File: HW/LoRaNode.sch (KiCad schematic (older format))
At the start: 3 parts

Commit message: update some schematic design
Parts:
- added C1, C2, C3, C5: 100nF, Capacitor_SMD:C_0402_1005Metric, symbol pspice:CAP
- added C4: 4u7, Capacitor_SMD:C_0603_1608Metric, symbol pspice:CAP
- added J1: Conn_ARM_JTAG_SWD_10, Connector_PinHeader_1.27mm:PinHeader_2x05_P1.27mm_Vertical_SMD, symbol Connector:Conn_ARM_JTAG_SWD_10
- added R1, R2, R3: 0, Resistor_SMD:R_0402_1005Metric, symbol Device:R
- U3: renamed from U?; footprint (none) -> Package_SO:SO-8_3.9x4.9mm_P1.27mm
- gave numbers to parts that had none: 2
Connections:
- net labels added: GND, NRST, SPI1_CLK, SPI1_MISO, SPI1_MOSI, SPI1_NSS, SPI1_SCLK, SWDCLK, SWDIO
- wire segments 0 -> 42
- no-connect marks 0 -> 3
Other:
- moved on the sheet: U2

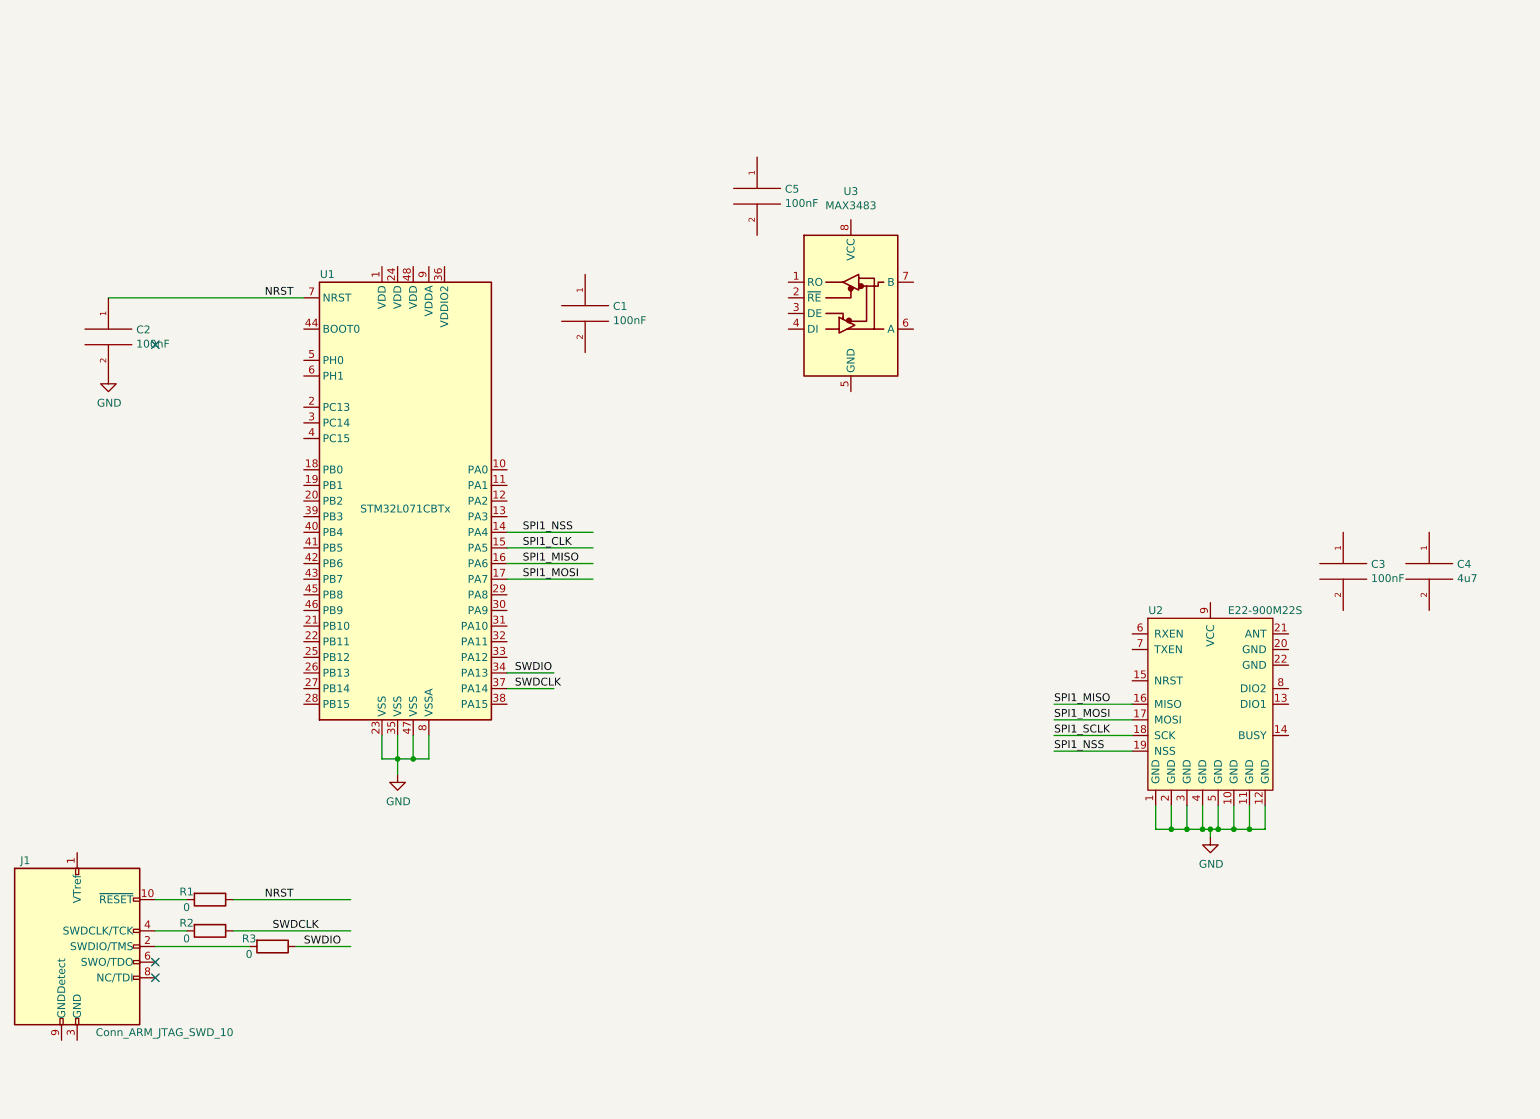
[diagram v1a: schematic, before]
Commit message: add crystal HSE/LSE into schematic
HSE -- 16MHz for high speed run mode
LSE -- 32.768KHz for low power mode, LPUART
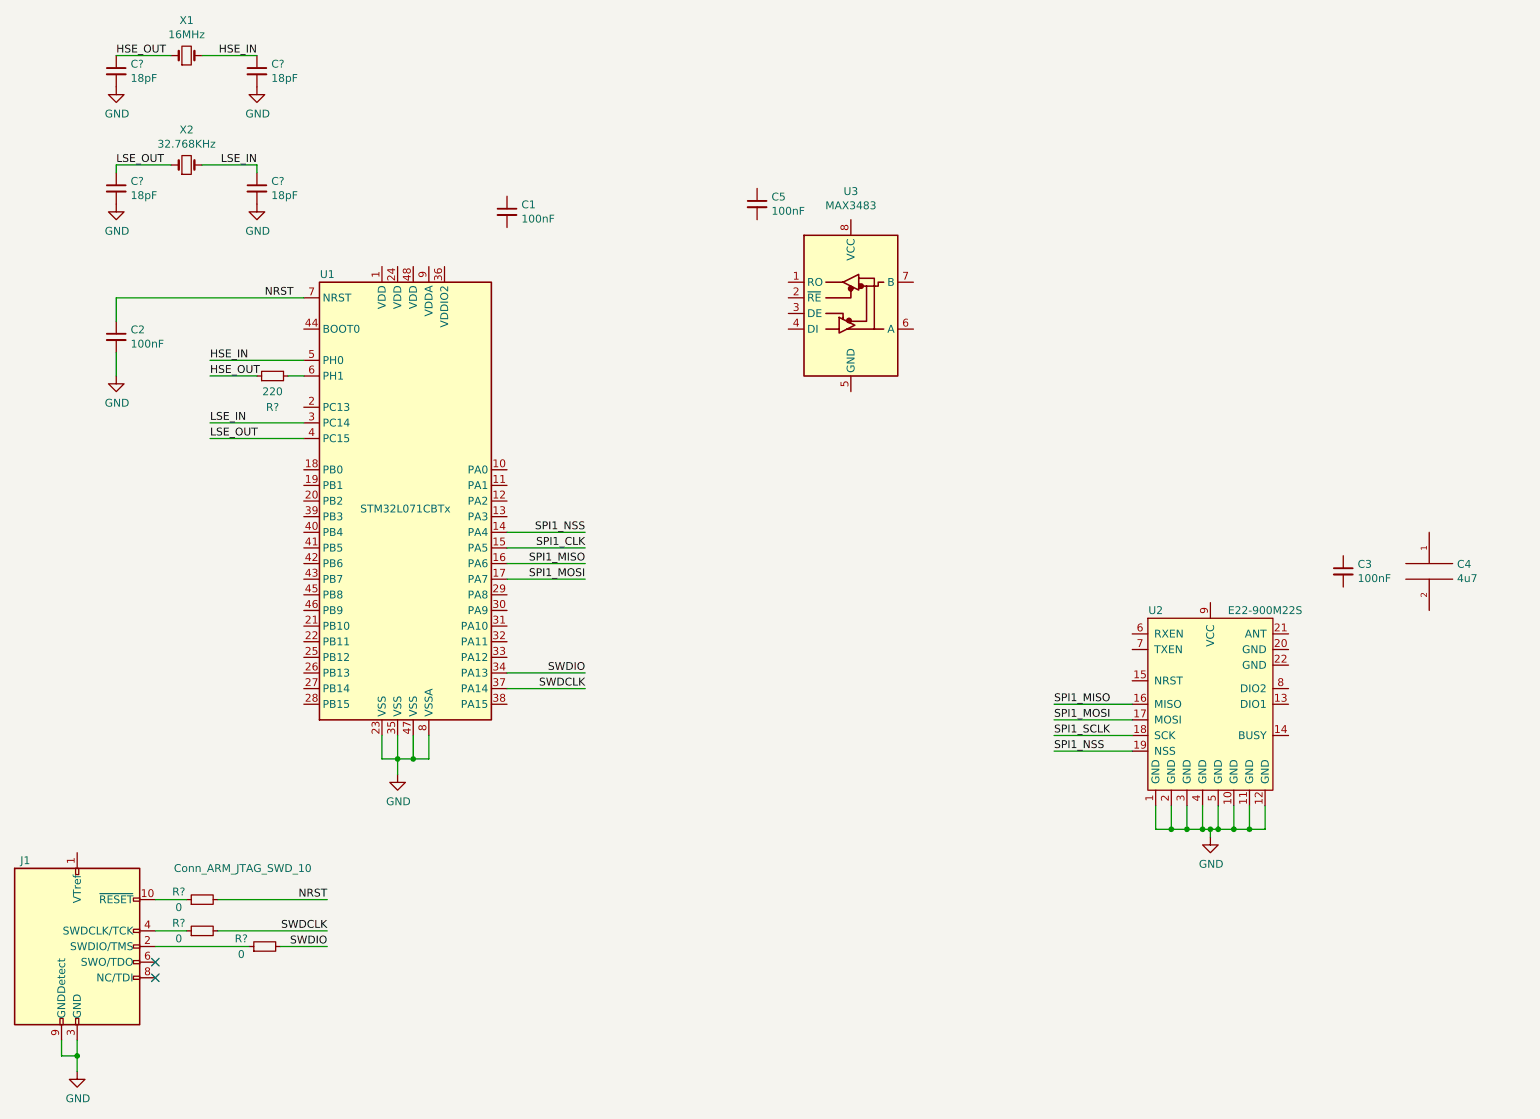
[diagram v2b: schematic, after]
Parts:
- removed C1, C2, C3, C5: 100nF, Capacitor_SMD:C_0402_1005Metric, symbol pspice:CAP
- removed R1, R2, R3: 0, Resistor_SMD:R_0402_1005Metric, symbol Device:R
- added C1, C2, C3, C5: 100nF, Capacitor_SMD:C_0402_1005Metric, symbol Device:C_Small
- added C? (x4): 18pF, Capacitor_SMD:C_0402_1005Metric, symbol Device:C_Small
- added R?: 220, Resistor_SMD:R_0402_1005Metric, symbol Device:R_Small
- added R? (x3): 0, Resistor_SMD:R_0402_1005Metric, symbol Device:R_Small
- added X1: 16MHz, Crystal:Crystal_SMD_HC49-SD, symbol Device:Crystal_Small
- added X2: 32.768KHz, symbol Device:Crystal_Small
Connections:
- net labels added: HSE_IN, HSE_OUT, LSE_IN, LSE_OUT
- wire segments 42 -> 59
- no-connect marks 3 -> 2

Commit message: update schematic & pcb files for design update
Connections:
- net LPUART1_TX: now reaches U1.12 (PA2)
- net LPUART1_RX: now reaches U1.13 (PA3)
- net USART1_RX: now reaches U3.1 (RO)
- net USART1_TX: now reaches U3.4 (DI)
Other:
- moved on the sheet: C5, U3
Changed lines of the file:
@@
 L Interface_UART:MAX3483 U3
 U 1 1 5E2F03A7
-P 6200 2400
-F 0 "U3" H 6200 3081 50  0000 C CNN
-F 1 "MAX3483" H 6200 2990 50  0000 C CNN
-F 2 "Package_SO:SO-8_3.9x4.9mm_P1.27mm" H 6200 1700 50  0001 C CNN
-F 3 "https://datasheets.maximintegrated.com/en/ds/MAX3483-MAX3491.pdf" H 6200 2450 50  0001 C CNN
-	1    6200 2400
+P 8600 2200
+F 0 "U3" H 8600 2881 50  0000 C CNN
+F 1 "MAX3483" H 8600 2790 50  0000 C CNN
+F 2 "Package_SO:SO-8_3.9x4.9mm_P1.27mm" H 8600 1500 50  0001 C CNN
+F 3 "https://datasheets.maximintegrated.com/en/ds/MAX3483-MAX3491.pdf" H 8600 2250 50  0001 C CNN
+	1    8600 2200
 	1    0    0    -1
 $EndComp
@@
 L Device:C_Small C5
 U 1 1 5E497E20
-P 5600 1800
-F 0 "C5" H 5692 1846 50  0000 L CNN
-F 1 "100nF" H 5692 1755 50  0000 L CNN
-F 2 "Capacitor_SMD:C_0402_1005Metric" H 5600 1800 50  0001 C CNN
-F 3 "~" H 5600 1800 50  0001 C CNN
-	1    5600 1800
+P 8000 1600
+F 0 "C5" H 8092 1646 50  0000 L CNN
+F 1 "100nF" H 8092 1555 50  0000 L CNN
+F 2 "Capacitor_SMD:C_0402_1005Metric" H 8000 1600 50  0001 C CNN
+F 3 "~" H 8000 1600 50  0001 C CNN
+	1    8000 1600
 	1    0    0    -1
 $EndComp
@@
 	1    0    0    -1
 $EndComp
+Wire Wire Line
+	8200 2100 7650 2100
+Wire Wire Line
+	8200 2400 7650 2400
+Text Label 7650 2400 0    50   ~ 0
+USART1_TX
+Text Label 7650 2100 0    50   ~ 0
+USART1_RX
+Wire Wire Line
+	4000 3700 4500 3700
+Wire Wire Line
+	4000 3800 4500 3800
+Text Label 4500 3800 2    50   ~ 0
+LPUART1_RX
+Text Label 4500 3700 2    50   ~ 0
+LPUART1_TX
 $EndSCHEMATC

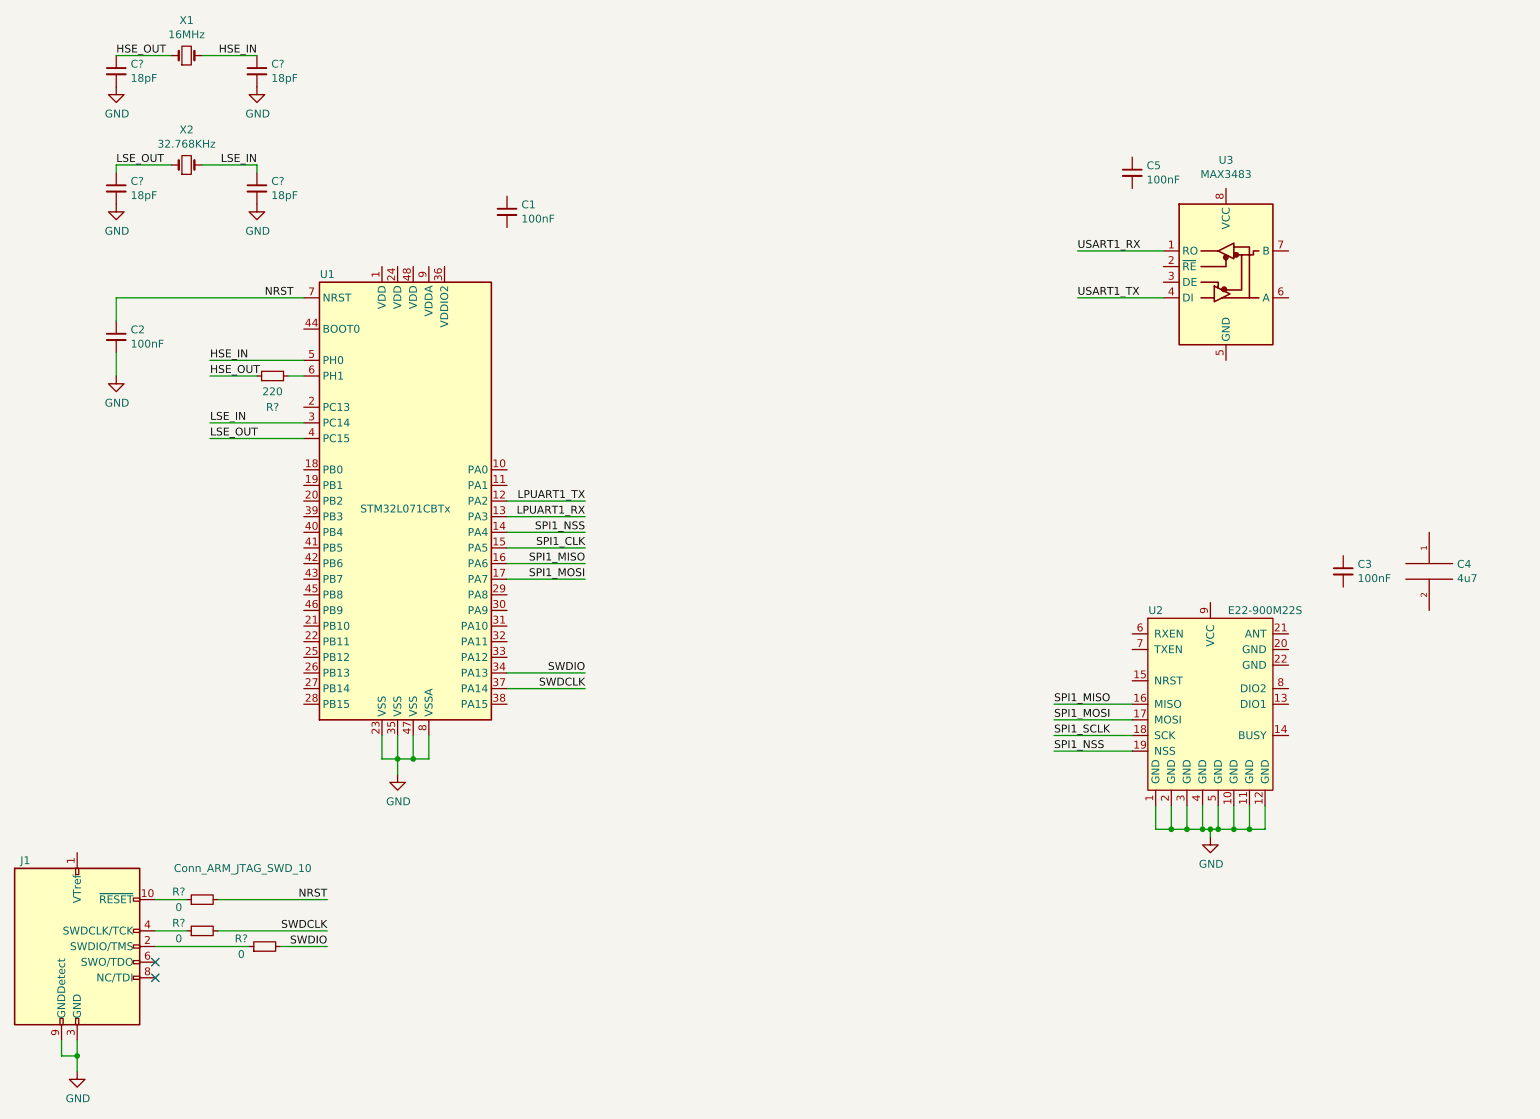
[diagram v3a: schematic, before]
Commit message: update schematic
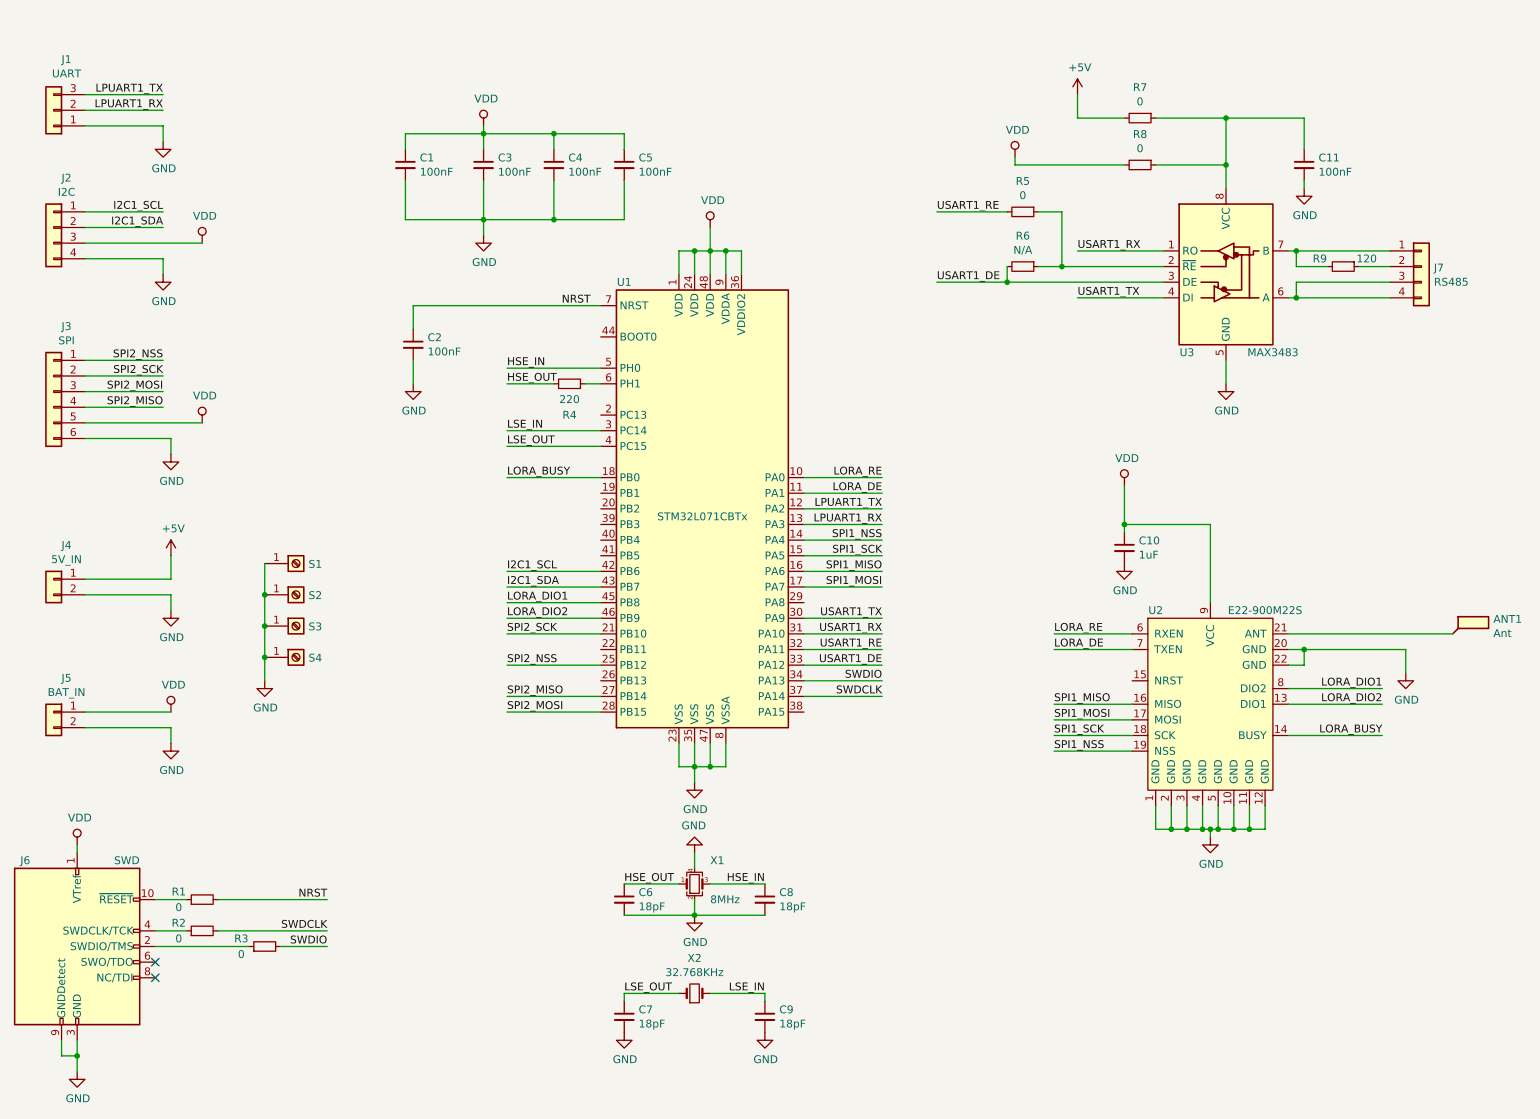
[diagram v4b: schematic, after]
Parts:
- removed C4: 4u7, Capacitor_SMD:C_0603_1608Metric, symbol pspice:CAP
- removed X1: 16MHz, Crystal:Crystal_SMD_HC49-SD, symbol Device:Crystal_Small
- added ANT1: Ant, TestPoint:TestPoint_Pad_2.0x2.0mm, symbol Connector:TestPoint_Flag
- added C10: 1uF, Capacitor_SMD:C_0603_1608Metric, symbol Device:C_Small
- added C4, C5: 100nF, Capacitor_SMD:C_0402_1005Metric, symbol Device:C_Small
- added J1: UART, Connector_PinSocket_2.00mm:PinSocket_1x03_P2.00mm_Vertical, symbol Connector_Generic:Conn_01x03
- added J2: I2C, Connector_PinSocket_2.00mm:PinSocket_1x04_P2.00mm_Vertical, symbol Connector_Generic:Conn_01x04
- added J3: SPI, Connector_PinSocket_2.00mm:PinSocket_1x06_P2.00mm_Vertical, symbol Connector_Generic:Conn_01x06
- added J4: 5V_IN, Connector_PinSocket_2.54mm:PinSocket_1x02_P2.54mm_Vertical, symbol Connector_Generic:Conn_01x02
- added J5: BAT_IN, Connector_PinSocket_2.54mm:PinSocket_1x02_P2.54mm_Vertical, symbol Connector_Generic:Conn_01x02
- added J7: RS485, Connector_PinHeader_2.54mm:PinHeader_1x04_P2.54mm_Vertical, symbol Connector_Generic:Conn_01x04
- added R5, R7, R8: 0, Resistor_SMD:R_0402_1005Metric, symbol Device:R_Small
- added R6: N/A, Resistor_SMD:R_0402_1005Metric, symbol Device:R_Small
- added R9: 120, Resistor_SMD:R_0603_1608Metric, symbol Device:R_Small
- added S1: S1, TestPoint:TestPoint_Plated_Hole_D3.0mm, symbol Connector:Screw_Terminal_01x01
- added S2: S2, TestPoint:TestPoint_Plated_Hole_D3.0mm, symbol Connector:Screw_Terminal_01x01
- added S3: S3, TestPoint:TestPoint_Plated_Hole_D3.0mm, symbol Connector:Screw_Terminal_01x01
- added S4: S4, TestPoint:TestPoint_Plated_Hole_D3.0mm, symbol Connector:Screw_Terminal_01x01
- added X1: 8MHz, Crystal:Crystal_SMD_TXC_7M-4Pin_3.2x2.5mm, symbol Device:Crystal_GND24_Small
- J6: renamed from J1; value Conn_ARM_JTAG_SWD_10 -> SWD
- X2: footprint (none) -> Crystal:Crystal_SMD_3215-2Pin_3.2x1.5mm
- gave numbers to parts that had none: 8
- renumbered C5 to C11
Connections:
- net SPI1_SCLK is gone; now on net SPI1_SCK: U2.18 (SCK)
- net GND: now also C1.2, C11.2, C3.2, U2.20 (GND), U2.22 (GND), U3.5 (GND), C10.2, C4.2, C5.2, J1.1 (Pin_1), J2.4 (Pin_4), J3.6 (Pin_6), J4.2 (Pin_2), J5.2 (Pin_2), S1.1 (Pin_1), S2.1 (Pin_1), S3.1 (Pin_1), S4.1 (Pin_1), X1.2, X1.4
- net HSE_IN: now also X1.3
- net HSE_OUT: now also X1.1
- net LPUART1_RX: now also J1.2 (Pin_2)
- net LPUART1_TX: now also J1.3 (Pin_3)
- net USART1_RX: now also U1.31 (PA10)
- net USART1_TX: now also U1.30 (PA9)
- net VDD: now reaches U1.1 (VDD)
- net VDD: now also C1.1, C3.1, J6.1 (VTref), U1.24 (VDD), U1.36 (VDDIO2), U1.48 (VDD), U1.9 (VDDA), U2.9 (VCC), C10.1, C4.1, C5.1, J2.3 (Pin_3), J3.5 (Pin_5), J5.1 (Pin_1), R8.2
- net LORA_RE: now reaches U1.10 (PA0)
- net LORA_RE: now also U2.6 (RXEN)
- net LORA_DE: now reaches U1.11 (PA1)
- net LORA_DE: now also U2.7 (TXEN)
- net LORA_BUSY: now reaches U1.18 (PB0)
- net LORA_BUSY: now also U2.14 (BUSY)
- net SPI2_SCK: now reaches U1.21 (PB10)
- net SPI2_SCK: now also J3.2 (Pin_2)
- net SPI2_NSS: now reaches U1.25 (PB12)
- net SPI2_NSS: now also J3.1 (Pin_1)
- net SPI2_MISO: now reaches U1.27 (PB14)
- net SPI2_MISO: now also J3.4 (Pin_4)
- net SPI2_MOSI: now reaches U1.28 (PB15)
- net SPI2_MOSI: now also J3.3 (Pin_3)
- net USART1_RE: now reaches U1.32 (PA11)
- net USART1_RE: now also R5.2
- net USART1_DE: now reaches U1.33 (PA12)
- net USART1_DE: now also U3.3 (DE), R6.2
- net I2C1_SCL: now reaches U1.42 (PB6)
- net I2C1_SCL: now also J2.1 (Pin_1)
- net I2C1_SDA: now reaches U1.43 (PB7)
- net I2C1_SDA: now also J2.2 (Pin_2)
- net LORA_DIO1: now reaches U1.45 (PB8)
- net LORA_DIO1: now also U2.8 (DIO2)
- net LORA_DIO2: now reaches U1.46 (PB9)
- net LORA_DIO2: now also U2.13 (DIO1)
- net at U3.2 (~RE): now also R5.1, R6.1
- net at U3.6 (A): now also J7.3 (Pin_3), J7.4 (Pin_4)
- net at U3.7 (B): now also J7.1 (Pin_1), R9.2
- net at U3.8 (VCC): now also C11.1, R7.1, R8.1
- net at U2.21 (ANT): now also ANT1.1
- net SPI1_CLK renamed SPI1_SCK
- new net: J7.2 (Pin_2), R9.1
- new net +5V: J4.1 (Pin_1), R7.2
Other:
- moved on the sheet: C1, C11, C2, C6, C7, C8, C9, R4, U1, X2
